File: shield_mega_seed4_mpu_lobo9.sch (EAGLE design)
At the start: 35 parts, among them U1 GY-521MPU6050

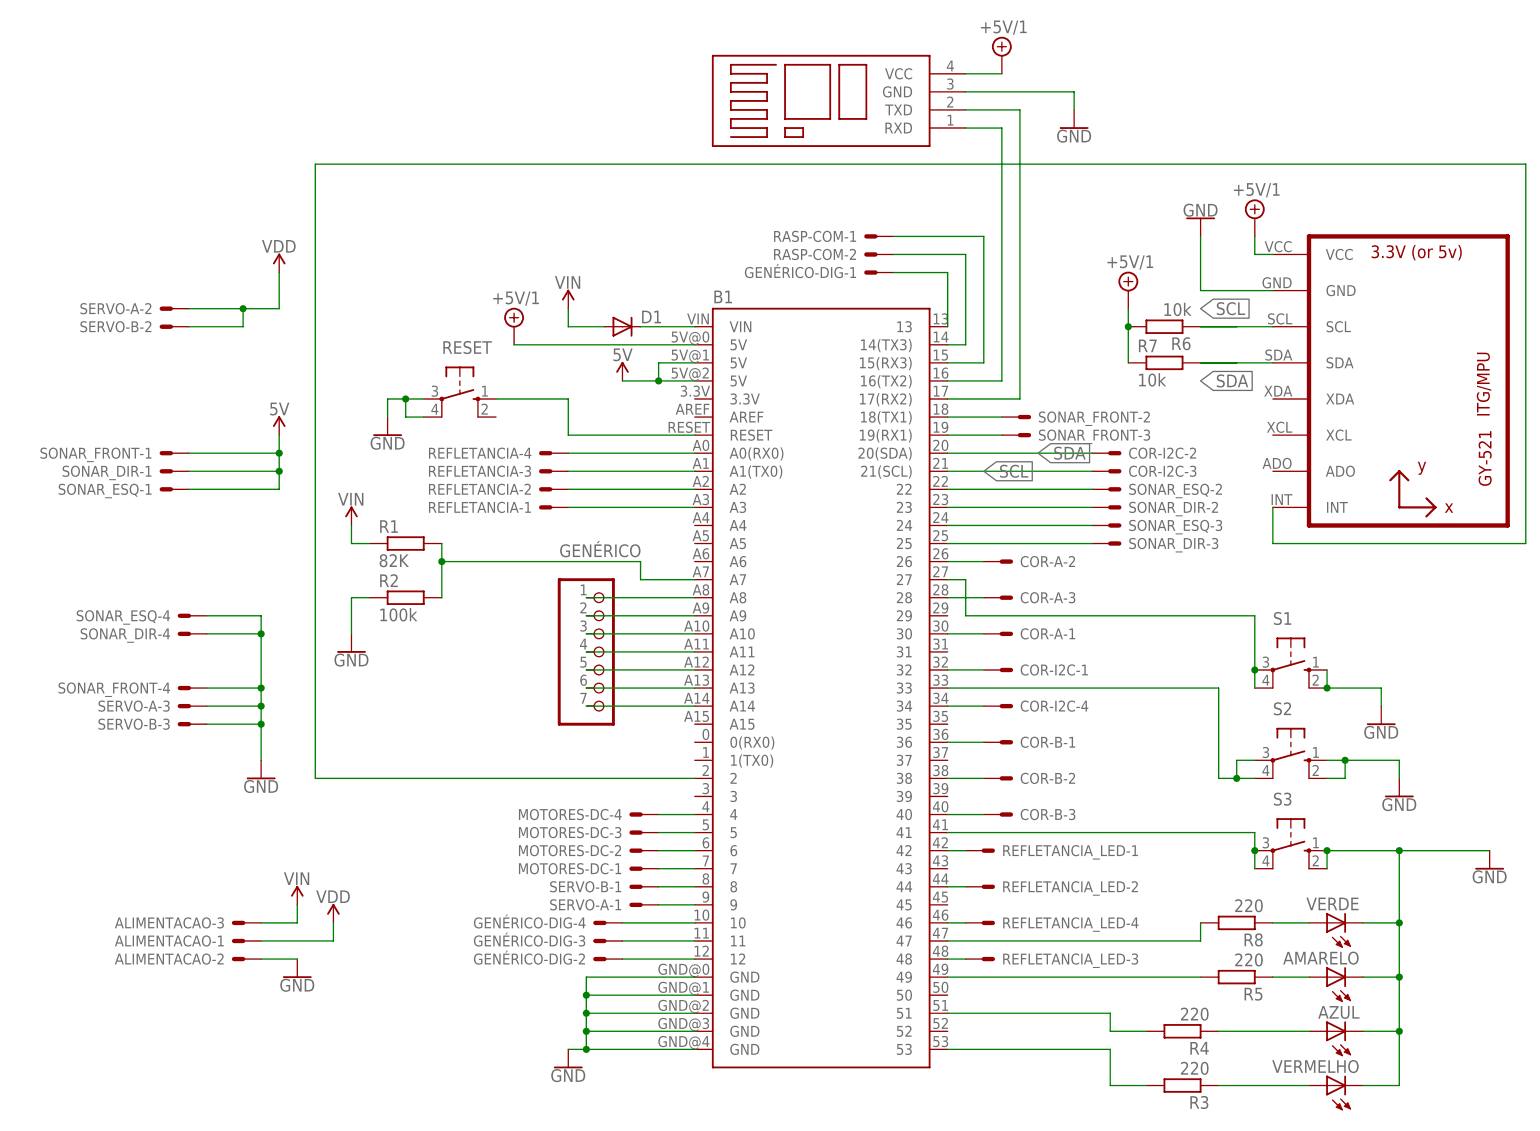
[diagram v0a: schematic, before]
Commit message: Mudança de botões
mudança de posição nos botões
adição de conectores genéricos
adição de um quarto conector para sonares
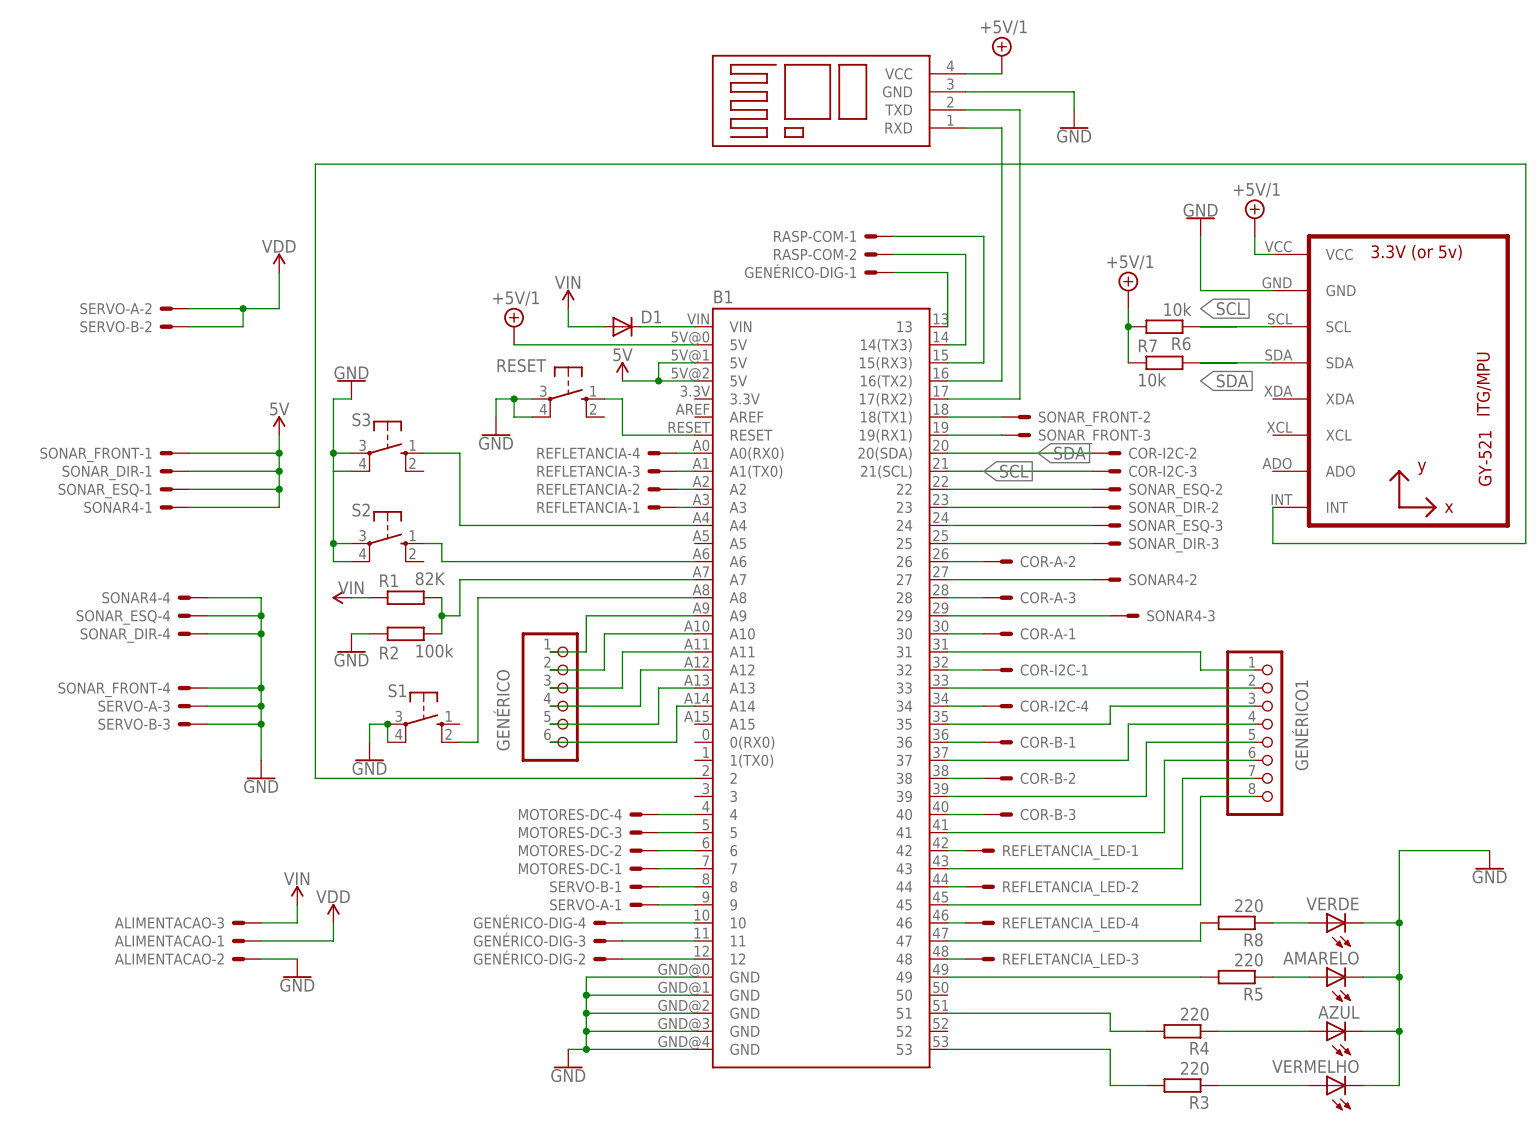
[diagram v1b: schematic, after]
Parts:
- added GENÉRICO1: (no value), pinhead:PINHD-1X8
- added SONAR4: 22-23-2041, con-molex:22-23-2041
- GENÉRICO: device pinhead:PINHD-1X7 -> pinhead:PINHD-1X6
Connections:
- new net N$59: B1.A4, S3.S
- new net N$60: B1.31, GENÉRICO1.1
- new net N$61: B1.33, GENÉRICO1.2
- new net N$62: B1.35, GENÉRICO1.3
- new net N$63: B1.37, GENÉRICO1.4
- new net N$64: B1.39, GENÉRICO1.5
- new net N$65: B1.41, GENÉRICO1.6
- new net N$66: B1.43, GENÉRICO1.7
- new net N$67: B1.45, GENÉRICO1.8
- net 5V: now also SONAR4-1.S
- net GND: now also S1.P, S1.P1, S2.P, S2.P1, S3.P, S3.P1, SONAR4-4.S; no longer S1.S, S1.S1, S2.S, S2.S1, S3.S, S3.S1
- net N$27: now also B1.27, SONAR4-2.S; no longer B1.33, S2.P, S2.P1
- net N$28: now also B1.A6, S2.S; no longer B1.27, S1.P, S1.P1
- net N$30: now also B1.29, SONAR4-3.S; no longer B1.41, S3.P, S3.P1
- net N$52: now also B1.A14, GENÉRICO.6; no longer B1.A8, GENÉRICO.1
- net N$53: now also B1.A13, GENÉRICO.5; no longer B1.A9, GENÉRICO.2
- net N$54: now also B1.A12, GENÉRICO.4; no longer B1.A10, GENÉRICO.3
- net N$55: now also GENÉRICO.3; no longer GENÉRICO.4
- net N$56: now also B1.A10, GENÉRICO.2; no longer B1.A12, GENÉRICO.5
- net N$57: now also B1.A9, GENÉRICO.1; no longer B1.A13, GENÉRICO.6
- net N$58: now also B1.A8, S1.S1; no longer B1.A14, GENÉRICO.7
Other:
- moved on the sheet: R1, R2, REFLETANCIA-1, REFLETANCIA-2, REFLETANCIA-3, REFLETANCIA-4, RESET, S1, S2, S3

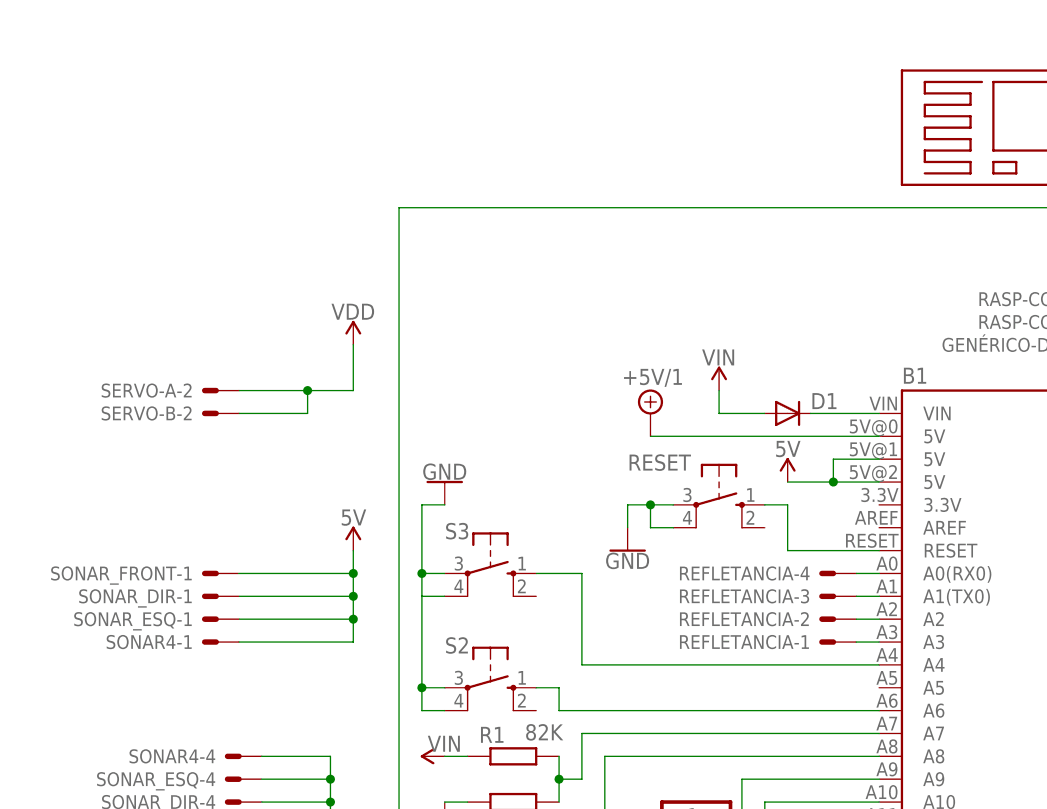
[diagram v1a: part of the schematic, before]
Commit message: Adição de conectores
Adição dos conectores de alimentação genéricos
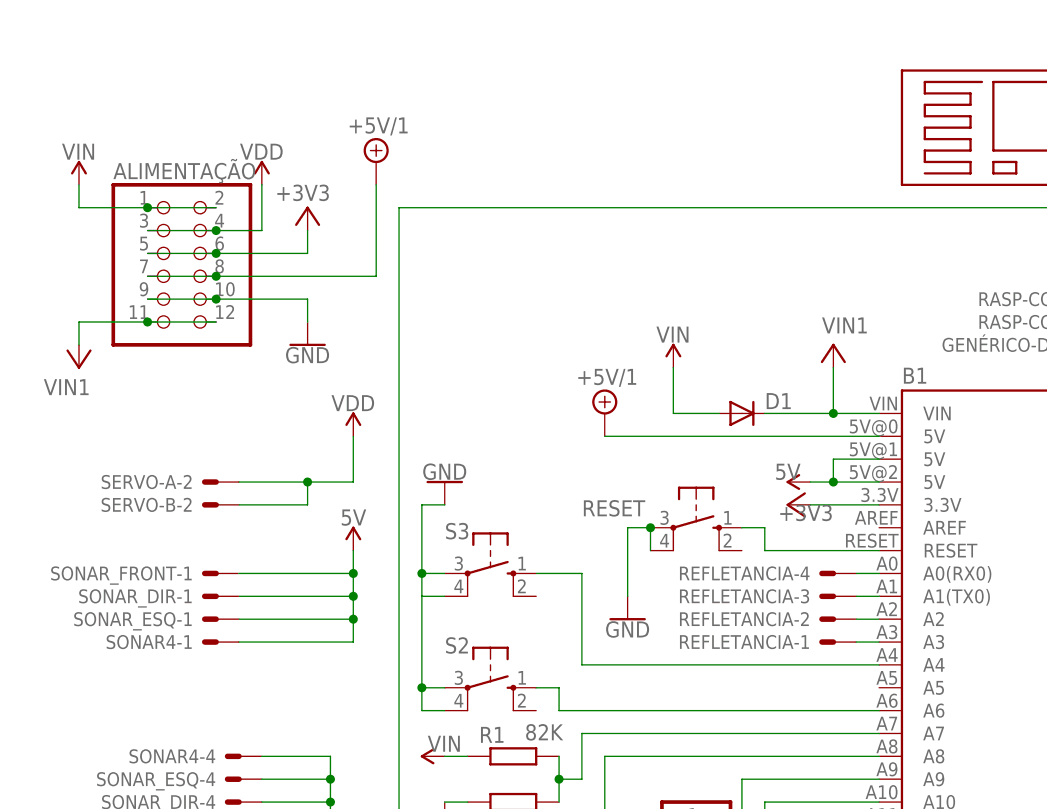
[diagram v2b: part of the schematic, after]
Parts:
- added ALIMENTAÇÃO: (no value), pinhead:PINHD-2X6
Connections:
- removed net N$32: B1.VIN, D1.C
- new net +3V3: ALIMENTAÇÃO.5, ALIMENTAÇÃO.6, B1.3.3V
- new net V+: ALIMENTAÇÃO.11, ALIMENTAÇÃO.12, B1.VIN, D1.C
- net +5V/1: now also ALIMENTAÇÃO.7, ALIMENTAÇÃO.8
- net GND: now also ALIMENTAÇÃO.10, ALIMENTAÇÃO.9
- net VDD: now also ALIMENTAÇÃO.3, ALIMENTAÇÃO.4
- net VIN: now also ALIMENTAÇÃO.1, ALIMENTAÇÃO.2
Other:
- moved on the sheet: D1, RESET, SERVO-A-2, SERVO-B-2

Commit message: Adição de logo
modificação de logo do IF
adição na parte superior da placa de logos da robótica
adição de imagens dos logos
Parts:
- added GENÉRICO2: (no value), pinhead:PINHD-1X3
- renumbered GENÉRICO-DIG to GENÉRICO3
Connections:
- new net N$32: B1.0(RX0), GENÉRICO2.1
- new net N$68: B1.1(TX0), GENÉRICO2.2
- new net N$69: B1.3, GENÉRICO2.3
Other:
- moved on the sheet: GENÉRICO
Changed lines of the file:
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@@
 <part name="SUPPLY5" library="supply2" deviceset="+5V/1" device=""/>
 <part name="GND4" library="SparkFun-PowerSymbols" deviceset="GND" device=""/>
-<part name="GENÉRICO-DIG" library="con-molex" deviceset="22-23-2041" device="" value=""/>
+<part name="GENÉRICO3" library="con-molex" deviceset="22-23-2041" device="" value=""/>
 <part name="COR-B" library="con-molex" deviceset="22-23-2031" device="" value=""/>
 <part name="REFLETANCIA_LED" library="con-molex" deviceset="22-23-2041" device="" value=""/>
@@
 <part name="SUPPLY15" library="supply2" library_urn="urn:adsk.eagle:library:372" deviceset="V+" device="" value="VIN1"/>
 <part name="SUPPLY16" library="supply2" library_urn="urn:adsk.eagle:library:372" deviceset="V+" device="" value="VIN1"/>
+<part name="GENÉRICO2" library="pinhead" library_urn="urn:adsk.eagle:library:325" deviceset="PINHD-1X3" device="" package3d_urn="urn:adsk.eagle:package:22458/2"/>
 </parts>
 <sheets>
@@
 <attribute name="VALUE" x="119.38" y="124.206" size="1.778" layer="96" align="top-center"/>
 </instance>
-<instance part="GENÉRICO-DIG" gate="-1" x="91.44" y="104.14" smashed="yes" rot="R180">
+<instance part="GENÉRICO3" gate="-1" x="91.44" y="104.14" smashed="yes" rot="R180">
 <attribute name="NAME" x="88.9" y="104.902" size="1.524" layer="95" rot="R180"/>
 <attribute name="VALUE" x="92.202" y="102.743" size="1.778" layer="96" rot="R180"/>
 </instance>
-<instance part="GENÉRICO-DIG" gate="-2" x="53.34" y="7.62" smashed="yes" rot="R180">
+<instance part="GENÉRICO3" gate="-2" x="53.34" y="7.62" smashed="yes" rot="R180">
 <attribute name="NAME" x="50.8" y="8.382" size="1.524" layer="95" rot="R180"/>
 </instance>
-<instance part="GENÉRICO-DIG" gate="-3" x="53.34" y="10.16" smashed="yes" rot="R180">
+<instance part="GENÉRICO3" gate="-3" x="53.34" y="10.16" smashed="yes" rot="R180">
 <attribute name="NAME" x="50.8" y="10.922" size="1.524" layer="95" rot="R180"/>
 </instance>
-<instance part="GENÉRICO-DIG" gate="-4" x="53.34" y="12.7" smashed="yes" rot="R180">
+<instance part="GENÉRICO3" gate="-4" x="53.34" y="12.7" smashed="yes" rot="R180">
 <attribute name="NAME" x="50.8" y="13.462" size="1.524" layer="95" rot="R180"/>
 </instance>
@@
 <attribute name="NAME" x="109.22" y="11.938" size="1.524" layer="95"/>
 </instance>
-<instance part="GENÉRICO" gate="A" x="48.26" y="43.18" smashed="yes">
-<attribute name="NAME" x="40.005" y="36.83" size="1.778" layer="95" rot="R90"/>
-<attribute name="VALUE" x="41.91" y="30.48" size="1.778" layer="96"/>
+<instance part="GENÉRICO" gate="A" x="58.42" y="48.26" smashed="yes">
+<attribute name="NAME" x="50.165" y="41.91" size="1.778" layer="95" rot="R90"/>
+<attribute name="VALUE" x="52.07" y="35.56" size="1.778" layer="96"/>
 </instance>
 <instance part="GND5" gate="1" x="17.78" y="88.9" smashed="yes" rot="R180">
@@
 <instance part="SUPPLY16" gate="1" x="60.96" y="104.14" smashed="yes">
 <attribute name="VALUE" x="59.69" y="105.41" size="1.778" layer="96"/>
+</instance>
+<instance part="GENÉRICO2" gate="A" x="48.26" y="33.02" smashed="yes">
+<attribute name="NAME" x="40.005" y="24.13" size="1.778" layer="95" rot="R90"/>
+<attribute name="VALUE" x="41.91" y="25.4" size="1.778" layer="96"/>
 </instance>
 </instances>
@@
 <wire x1="182.88" y1="66.04" x2="182.88" y2="119.38" width="0.1524" layer="91"/>
 <wire x1="182.88" y1="119.38" x2="12.7" y2="119.38" width="0.1524" layer="91"/>
-<wire x1="12.7" y1="119.38" x2="12.7" y2="33.02" width="0.1524" layer="91"/>
-<wire x1="12.7" y1="33.02" x2="66.04" y2="33.02" width="0.1524" layer="91"/>
+<wire x1="12.7" y1="119.38" x2="12.7" y2="22.86" width="0.1524" layer="91"/>
 <pinref part="B1" gate="G$1" pin="2"/>
+<wire x1="66.04" y1="33.02" x2="53.34" y2="33.02" width="0.1524" layer="91"/>
+<wire x1="53.34" y1="33.02" x2="53.34" y2="22.86" width="0.1524" layer="91"/>
+<wire x1="12.7" y1="22.86" x2="53.34" y2="22.86" width="0.1524" layer="91"/>
 </segment>
 </net>
@@
 <segment>
 <pinref part="B1" gate="G$1" pin="12"/>
-<pinref part="GENÉRICO-DIG" gate="-2" pin="S"/>
+<pinref part="GENÉRICO3" gate="-2" pin="S"/>
 <wire x1="55.88" y1="7.62" x2="66.04" y2="7.62" width="0.1524" layer="91"/>
 </segment>
@@
 <segment>
 <pinref part="B1" gate="G$1" pin="11"/>
-<pinref part="GENÉRICO-DIG" gate="-3" pin="S"/>
+<pinref part="GENÉRICO3" gate="-3" pin="S"/>
 <wire x1="55.88" y1="10.16" x2="66.04" y2="10.16" width="0.1524" layer="91"/>
 </segment>
@@
 <segment>
 <pinref part="B1" gate="G$1" pin="10"/>
-<pinref part="GENÉRICO-DIG" gate="-4" pin="S"/>
+<pinref part="GENÉRICO3" gate="-4" pin="S"/>
 <wire x1="55.88" y1="12.7" x2="66.04" y2="12.7" width="0.1524" layer="91"/>
 </segment>
@@
 <net name="N$47" class="0">
 <segment>
-<pinref part="GENÉRICO-DIG" gate="-1" pin="S"/>
+<pinref part="GENÉRICO3" gate="-1" pin="S"/>
 <pinref part="B1" gate="G$1" pin="13"/>
 <wire x1="93.98" y1="104.14" x2="101.6" y2="104.14" width="0.1524" layer="91"/>
@@
 <segment>
 <pinref part="B1" gate="G$1" pin="A14"/>
-<wire x1="66.04" y1="43.18" x2="63.5" y2="43.18" width="0.1524" layer="91"/>
-<wire x1="63.5" y1="43.18" x2="63.5" y2="38.1" width="0.1524" layer="91"/>
 <pinref part="GENÉRICO" gate="A" pin="6"/>
-<wire x1="63.5" y1="38.1" x2="45.72" y2="38.1" width="0.1524" layer="91"/>
+<wire x1="66.04" y1="43.18" x2="55.88" y2="43.18" width="0.1524" layer="91"/>
 </segment>
 </net>
@@
 <segment>
 <pinref part="B1" gate="G$1" pin="A13"/>
-<wire x1="66.04" y1="45.72" x2="60.96" y2="45.72" width="0.1524" layer="91"/>
-<wire x1="60.96" y1="45.72" x2="60.96" y2="40.64" width="0.1524" layer="91"/>
 <pinref part="GENÉRICO" gate="A" pin="5"/>
-<wire x1="60.96" y1="40.64" x2="45.72" y2="40.64" width="0.1524" layer="91"/>
+<wire x1="66.04" y1="45.72" x2="55.88" y2="45.72" width="0.1524" layer="91"/>
 </segment>
 </net>
@@
 <segment>
 <pinref part="GENÉRICO" gate="A" pin="4"/>
-<wire x1="45.72" y1="43.18" x2="58.42" y2="43.18" width="0.1524" layer="91"/>
-<wire x1="58.42" y1="43.18" x2="58.42" y2="48.26" width="0.1524" layer="91"/>
+<wire x1="55.88" y1="48.26" x2="66.04" y2="48.26" width="0.1524" layer="91"/>
 <pinref part="B1" gate="G$1" pin="A12"/>
-<wire x1="58.42" y1="48.26" x2="66.04" y2="48.26" width="0.1524" layer="91"/>
 </segment>
 </net>
@@
 <segment>
 <pinref part="GENÉRICO" gate="A" pin="3"/>
-<wire x1="45.72" y1="45.72" x2="55.88" y2="45.72" width="0.1524" layer="91"/>
-<wire x1="55.88" y1="45.72" x2="55.88" y2="50.8" width="0.1524" layer="91"/>
 <pinref part="B1" gate="G$1" pin="A11"/>
 <wire x1="55.88" y1="50.8" x2="66.04" y2="50.8" width="0.1524" layer="91"/>
@@
 <segment>
 <pinref part="GENÉRICO" gate="A" pin="2"/>
-<wire x1="45.72" y1="48.26" x2="53.34" y2="48.26" width="0.1524" layer="91"/>
-<wire x1="53.34" y1="48.26" x2="53.34" y2="53.34" width="0.1524" layer="91"/>
 <pinref part="B1" gate="G$1" pin="A10"/>
-<wire x1="53.34" y1="53.34" x2="66.04" y2="53.34" width="0.1524" layer="91"/>
+<wire x1="55.88" y1="53.34" x2="66.04" y2="53.34" width="0.1524" layer="91"/>
 </segment>
 </net>
@@
 <segment>
 <pinref part="GENÉRICO" gate="A" pin="1"/>
-<wire x1="45.72" y1="50.8" x2="50.8" y2="50.8" width="0.1524" layer="91"/>
-<wire x1="50.8" y1="50.8" x2="50.8" y2="55.88" width="0.1524" layer="91"/>
 <pinref part="B1" gate="G$1" pin="A9"/>
-<wire x1="50.8" y1="55.88" x2="66.04" y2="55.88" width="0.1524" layer="91"/>
+<wire x1="55.88" y1="55.88" x2="66.04" y2="55.88" width="0.1524" layer="91"/>
 </segment>
 </net>
@@
 </segment>
 </net>
+<net name="N$32" class="0">
+<segment>
+<pinref part="GENÉRICO2" gate="A" pin="1"/>
+<wire x1="45.72" y1="35.56" x2="45.72" y2="38.1" width="0.1524" layer="91"/>
+<pinref part="B1" gate="G$1" pin="0(RX0)"/>
+<wire x1="45.72" y1="38.1" x2="66.04" y2="38.1" width="0.1524" layer="91"/>
+</segment>
+</net>
+<net name="N$68" class="0">
+<segment>
+<pinref part="B1" gate="G$1" pin="1(TX0)"/>
+<wire x1="66.04" y1="35.56" x2="50.8" y2="35.56" width="0.1524" layer="91"/>
+<wire x1="50.8" y1="35.56" x2="50.8" y2="33.02" width="0.1524" layer="91"/>
+<pinref part="GENÉRICO2" gate="A" pin="2"/>
+<wire x1="50.8" y1="33.02" x2="45.72" y2="33.02" width="0.1524" layer="91"/>
+</segment>
+</net>
+<net name="N$69" class="0">
+<segment>
+<pinref part="B1" gate="G$1" pin="3"/>
+<pinref part="GENÉRICO2" gate="A" pin="3"/>
+<wire x1="66.04" y1="30.48" x2="45.72" y2="30.48" width="0.1524" layer="91"/>
+</segment>
+</net>
